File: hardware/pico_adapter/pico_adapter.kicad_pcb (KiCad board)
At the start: 2 copper layers, 97.8 x 83.8 mm, 43 parts, among them J1 L77HDE15SD1CH4F, J2 AudioJack3, J3 5V in, Q1 Q_NMOS_DGS, Q2 Q_NMOS_DGS

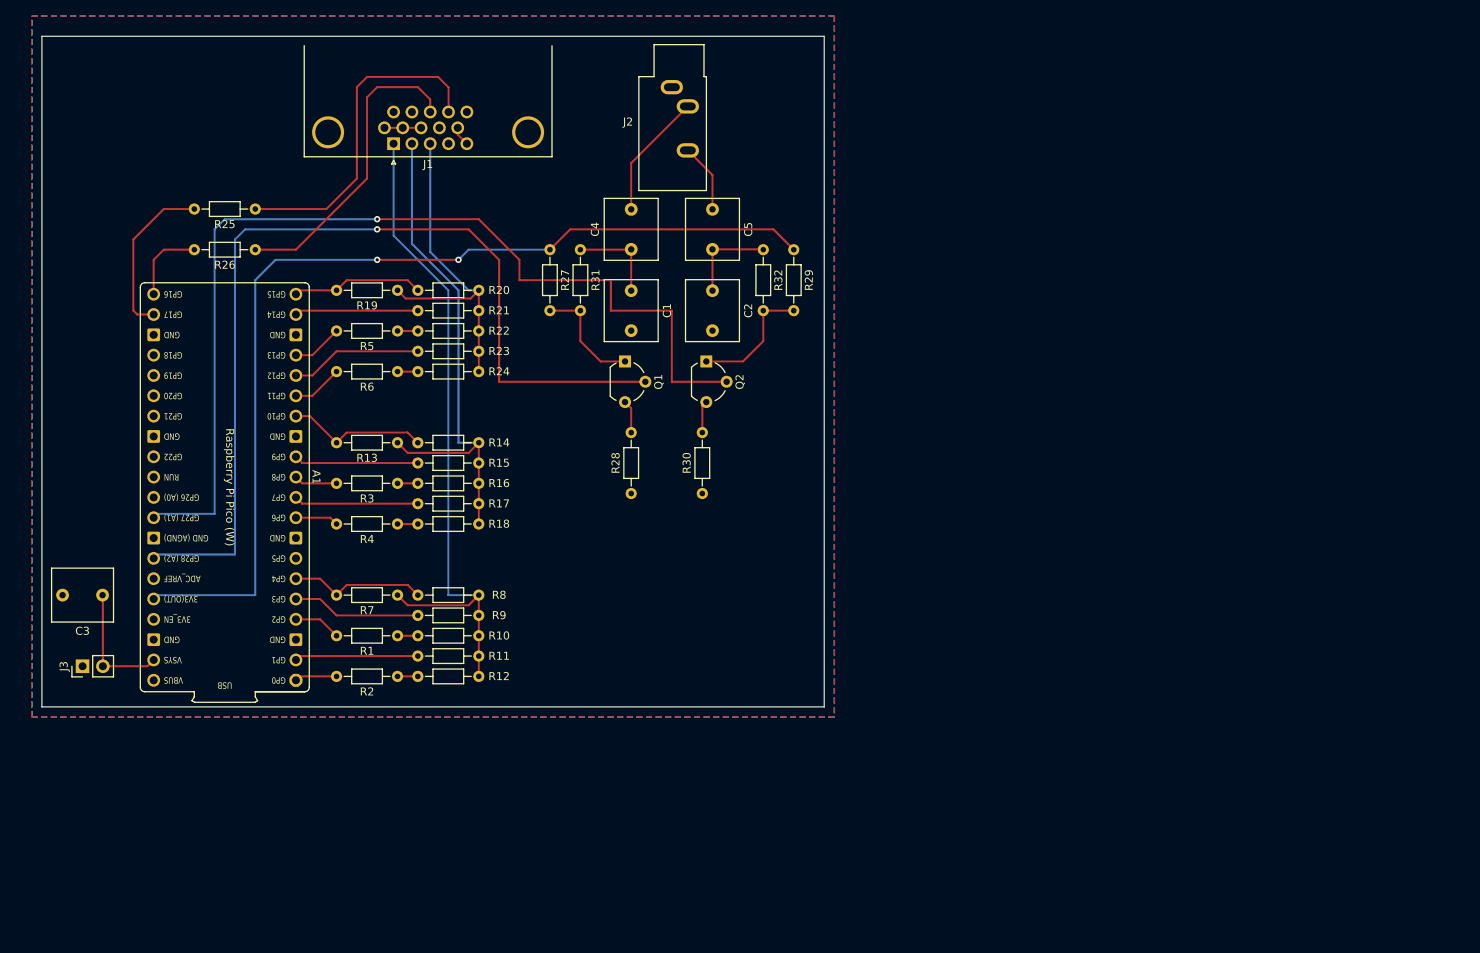
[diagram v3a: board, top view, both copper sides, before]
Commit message: UPDATED PICO FOOTPRINT [!] + smaller board
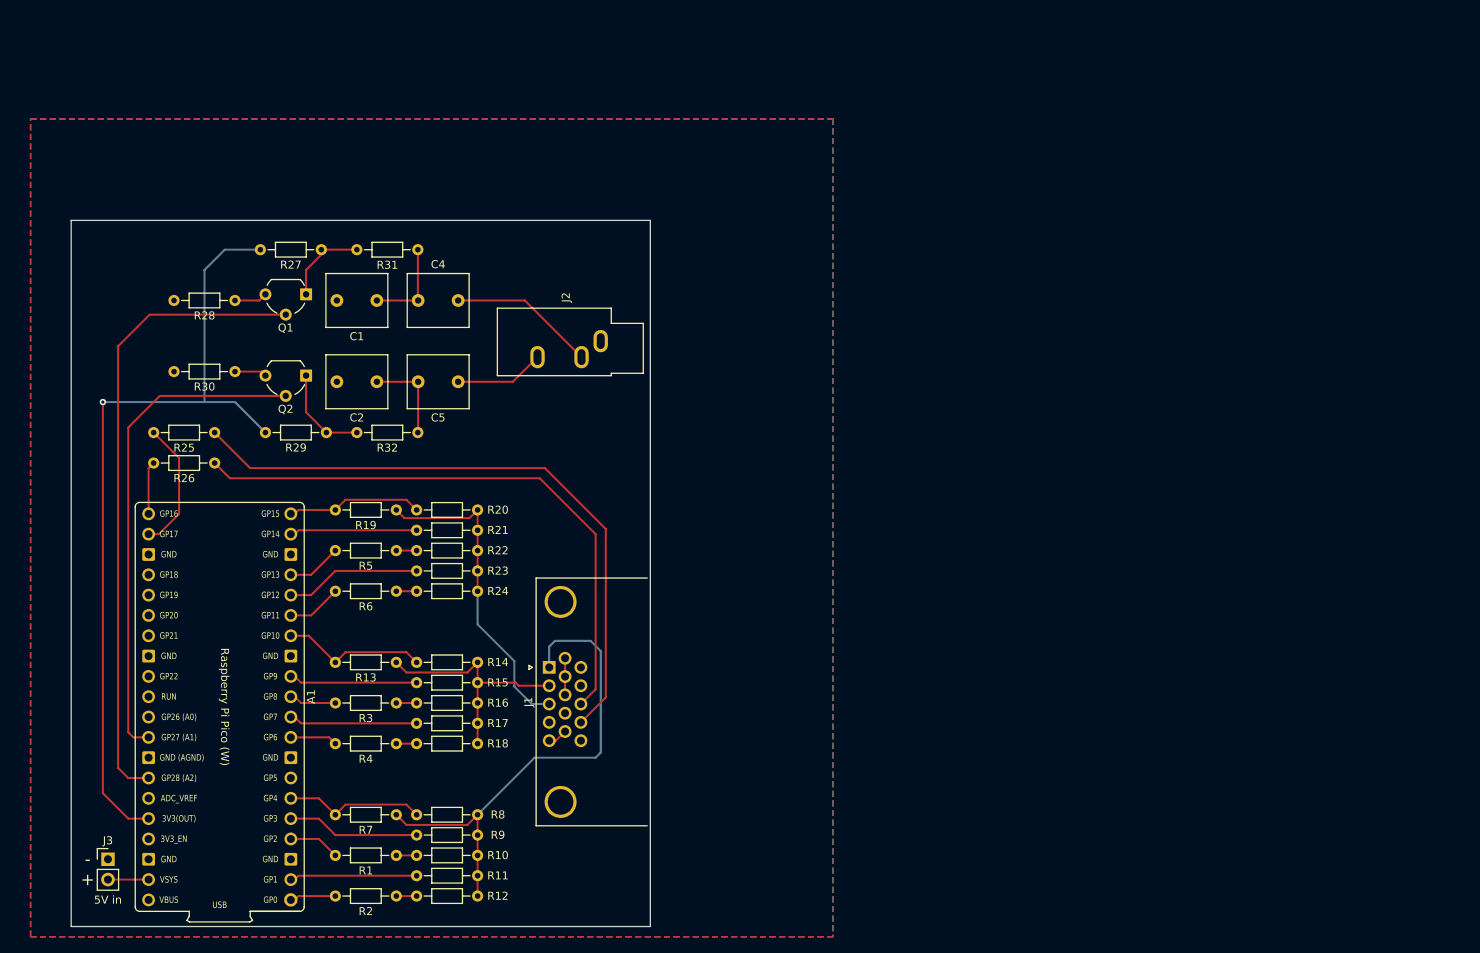
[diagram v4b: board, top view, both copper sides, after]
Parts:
- removed C3: 100n, Capacitor_THT:C_Rect_L7.5mm_W6.5mm_P5.00mm
- moved R29 69.9 mm to (59.7, 72.4), turned to 0 degrees
- moved J1 68.3 mm to (95.2, 101.7), turned to 90 degrees
- moved R30 67.8 mm to (48.3, 64.8), turned to 0 degrees
- moved R28 62.0 mm to (48.3, 55.9), turned to 0 degrees
- moved Q2 50.1 mm to (64.8, 65.3), turned to 180 degrees
- moved R32 48.9 mm to (78.7, 72.4), turned to 180 degrees
- moved C2 43.5 mm to (73.6, 66.0), turned to 180 degrees
- moved Q1 40.7 mm to (64.8, 55.1), turned to 180 degrees
- moved C5 38.4 mm to (83.8, 66.0), turned to 180 degrees
- moved R27 36.2 mm to (59.1, 49.5), turned to 0 degrees
- moved J2 33.0 mm to (101.6, 61.0), turned to -90 degrees
- moved C1 31.8 mm to (73.6, 55.9), turned to 180 degrees
- moved R25 28.4 mm to (53.3, 72.4)
- moved A1 27.5 mm to (62.9, 130.8)
- moved R18 27.5 mm to (86.2, 111.3)
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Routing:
- net /PWM_R: track 125.3 -> 62.2 mm, vias 1 -> 0
- net /PWM_L: track 118.7 -> 79.6 mm, vias 1 -> 0
- net /VSYNC: track 41.3 -> 79.3 mm
- net /HSYNC: track 38.4 -> 73.3 mm
- net /VGA_G: track 63.7 -> 30.5 mm
- net /VGA_R: track 84.4 -> 62.5 mm
- net +3V3: track 123.5 -> 102.4 mm, vias 2 -> 1
- net +5V: track 15.6 -> 5.08 mm
- net Net-(A1-Pad22): track 20.8 -> 16.3 mm
- net Net-(Q1-Pad1): track 14.3 -> 10.4 mm
- net Net-(Q2-Pad1): track 15.8 -> 12.0 mm
- net Net-(A1-Pad21): track 9.90 -> 6.61 mm
- net Net-(C5-Pad1): track 8.65 -> 11.2 mm
- net Net-(C4-Pad2): track 15.8 -> 18.4 mm
- net /VGA_B: track 42.8 -> 40.3 mm
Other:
- board size 97.8 x 83.8 mm -> 72.4 x 88.3 mm
- board text added: "+"
- board text added: "-"

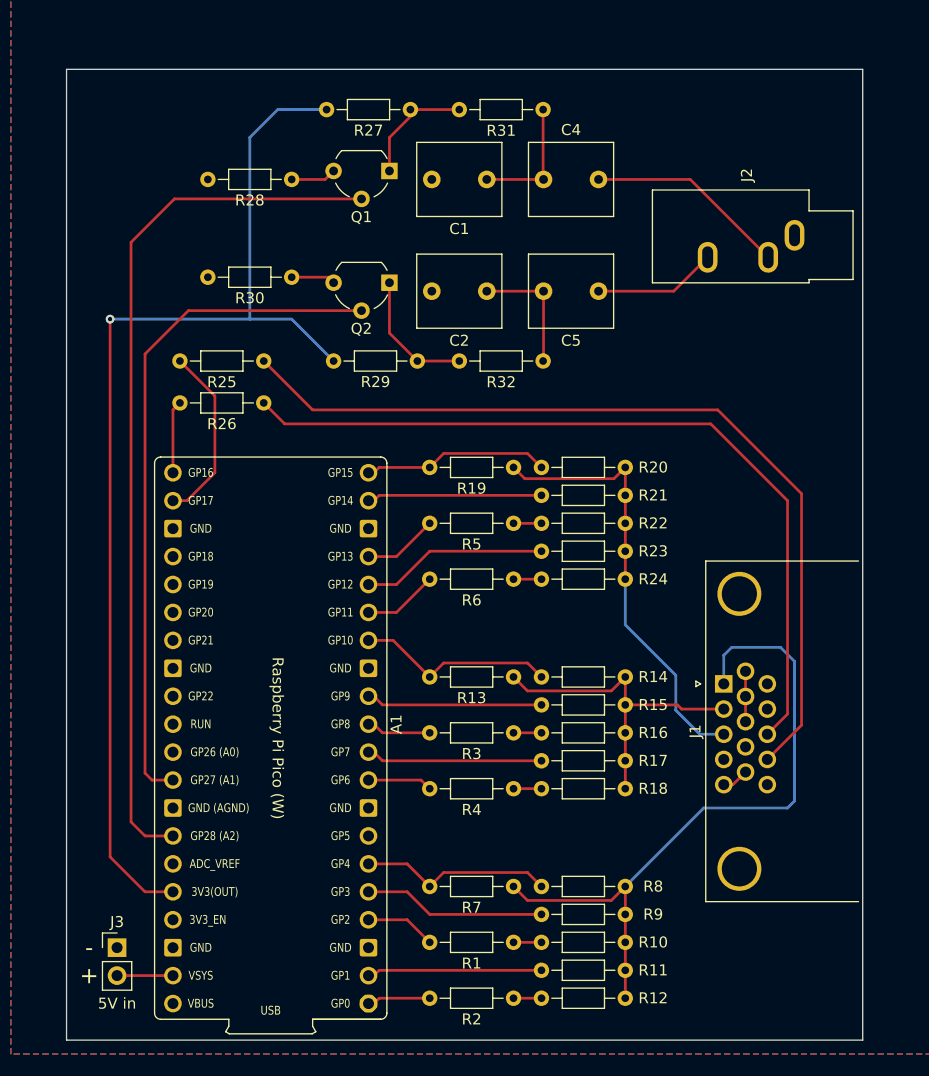
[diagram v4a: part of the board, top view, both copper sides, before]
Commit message: bigger resistors
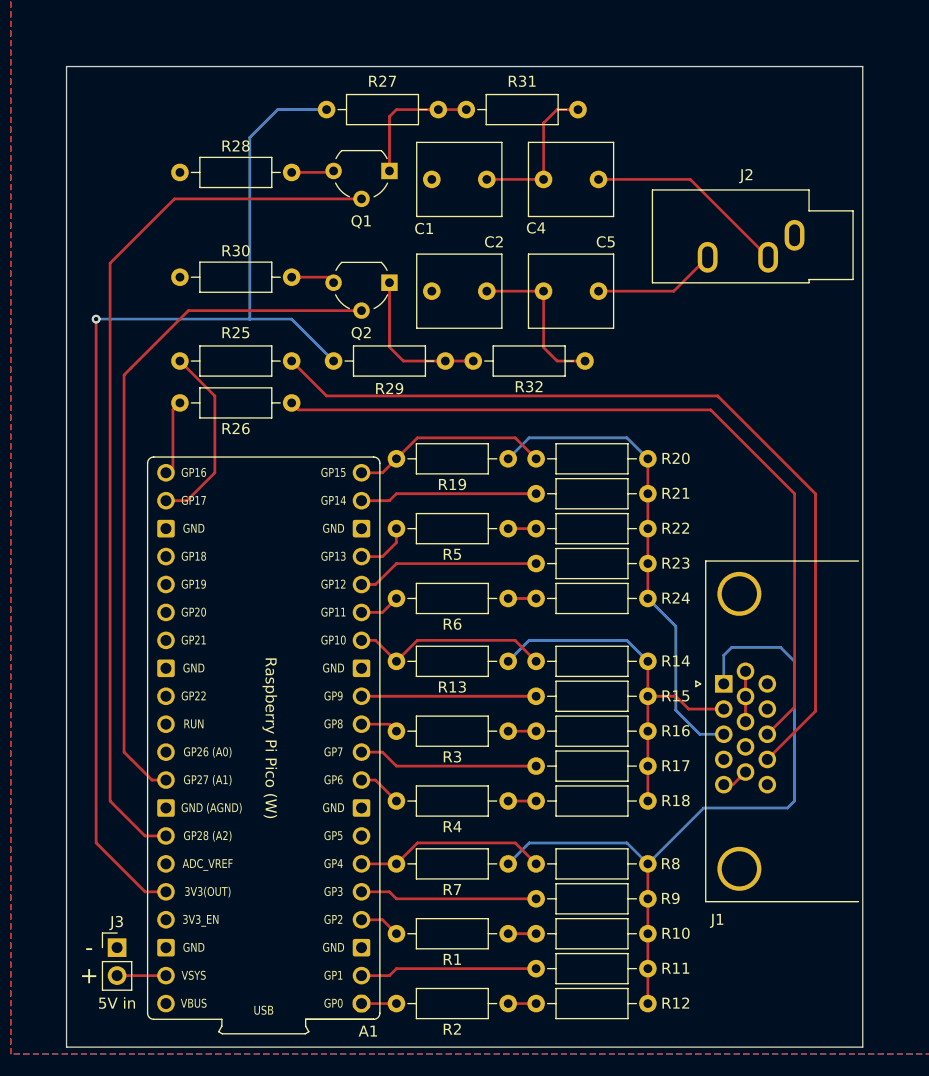
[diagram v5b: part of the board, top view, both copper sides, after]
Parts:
- R1, R10, R11, R12, R13, R14, R15, R16, R17, R18, R19, R2, R20, R21, R22, R23, R24, R25, R26, R27, R28, R29, R3, R30, R31, R32, R4, R5, R6, R7, R8, R9: footprint Resistor_THT:R_Axial_DIN0204_L3.6mm_D1.6mm_P7.62mm_Horizontal -> Resistor_THT:R_Axial_DIN0207_L6.3mm_D2.5mm_P10.16mm_Horizontal
- moved R32 3.81 mm to (82.5, 72.4)
- moved R31 3.18 mm to (81.9, 49.5)
- moved R8 2.91 mm to (88.3, 118.1)
- moved R24 2.70 mm to (88.3, 94.0)
- moved R28 2.62 mm to (45.7, 55.2)
- moved R25 2.54 mm to (55.9, 72.4)
- moved R26 2.54 mm to (55.9, 76.2)
- moved R30 2.54 mm to (45.7, 64.8)
- moved R14 2.50 mm to (88.3, 99.7)
- moved R9 2.50 mm to (88.3, 121.3)
- moved R23 2.34 mm to (88.3, 90.8)
- moved R18 2.34 mm to (88.3, 112.4)
- moved R10 2.20 mm to (88.3, 124.5)
- moved R15 2.20 mm to (88.3, 102.9)
- moved R20 2.20 mm to (88.3, 81.3)
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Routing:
- net /VGA_G: track 30.5 -> 34.4 mm
- net /VGA_B: track 40.3 -> 43.5 mm
- net Net-(C2-Pad1): track 11.5 -> 14.6 mm
- net /VGA_R: track 62.5 -> 65.2 mm
- net /GPIO11: track 6.33 -> 3.70 mm
- net Net-(C1-Pad1): track 11.5 -> 13.9 mm
- net /GPIO2: track 5.93 -> 3.70 mm
- net /GPIO0: track 5.28 -> 3.18 mm
- net Net-(Q2-Pad1): track 12.0 -> 14.0 mm
- net /GPIO8: track 5.41 -> 3.44 mm
- net Net-(Q1-Pad1): track 10.4 -> 12.2 mm
- net /GPIO15: track 16.5 -> 18.0 mm
- net /GPIO6: track 5.41 -> 3.96 mm
- net /GPIO13: track 6.33 -> 4.97 mm
- net /HSYNC: track 73.3 -> 72.0 mm
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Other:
- board size 72.4 x 88.3 mm -> 72.4 x 89.2 mm

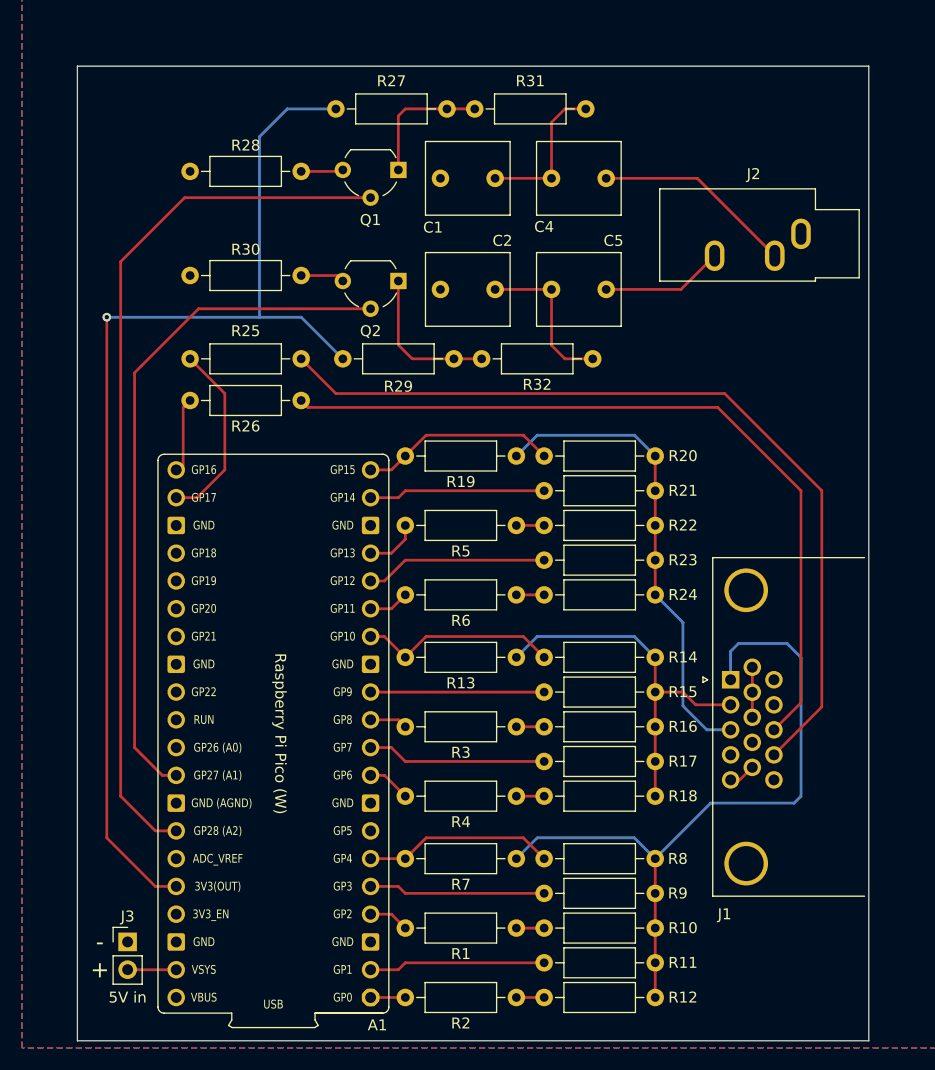
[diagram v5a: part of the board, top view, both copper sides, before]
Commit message: added addon-headers + reset button
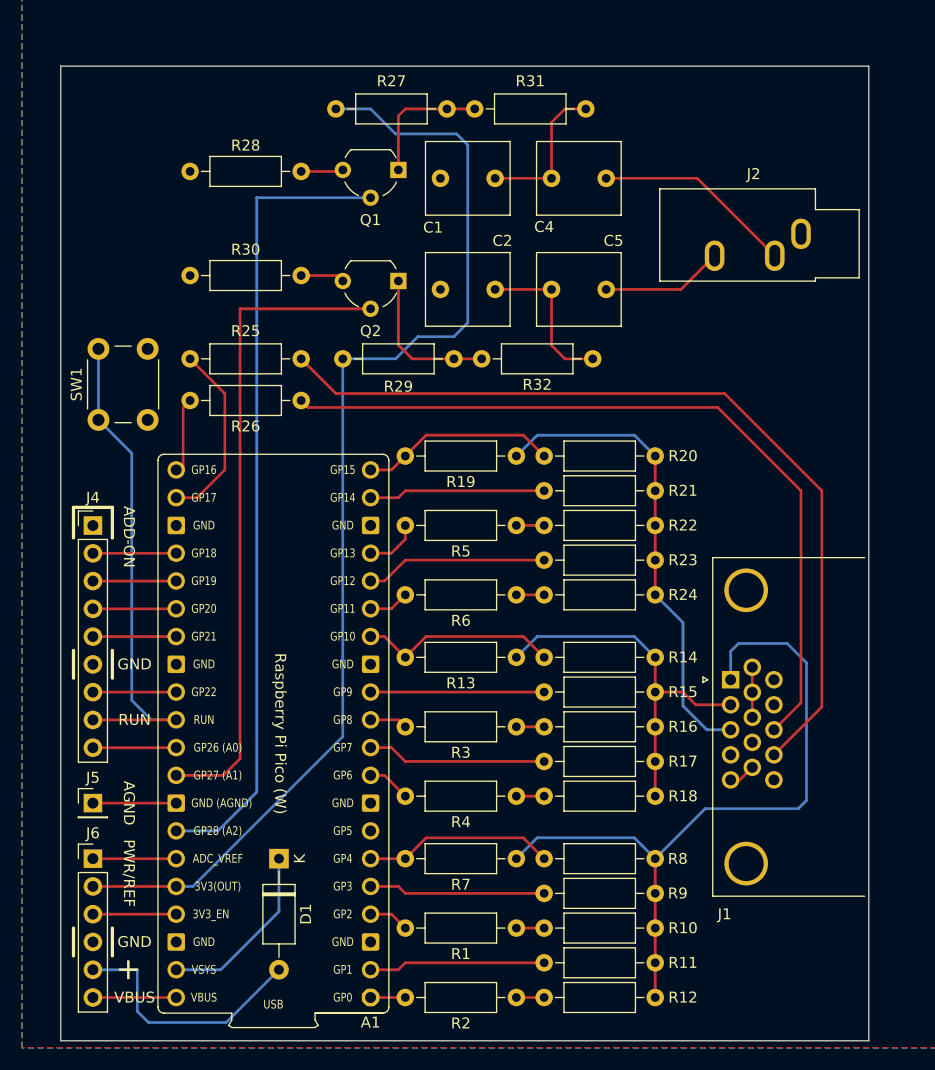
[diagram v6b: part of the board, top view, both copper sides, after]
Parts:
- removed J3: 5V in, Connector_PinHeader_2.54mm:PinHeader_1x02_P2.54mm_Vertical
- added D1: D_Schottky, Diode_THT:D_A-405_P10.16mm_Horizontal, F.Cu at (53.8, 118.1)
- added J4: ADD-ON, Connector_PinHeader_2.54mm:PinHeader_1x09_P2.54mm_Vertical, F.Cu at (36.8, 87.6)
- added J5: AGND, Connector_PinHeader_2.54mm:PinHeader_1x01_P2.54mm_Vertical, F.Cu at (36.8, 113.0)
- added J6: PWR_REF, Connector_PinHeader_2.54mm:PinHeader_1x06_P2.54mm_Vertical, F.Cu at (36.8, 118.1)
- added SW1: SW_Push, Button_Switch_THT:SW_PUSH_6mm_H5mm, F.Cu at (37.3, 78.0)
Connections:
- net Net-(A1-Pad21) renamed /GPIO16
- net Net-(A1-Pad22) renamed /GPIO17
- A1 pad 24: unconnected-(A1-Pad24) -> /GPIO18
- A1 pad 25: unconnected-(A1-Pad25) -> /GPIO19
- A1 pad 26: unconnected-(A1-Pad26) -> /GPIO20
- A1 pad 27: unconnected-(A1-Pad27) -> /GPIO21
- A1 pad 29: unconnected-(A1-Pad29) -> /GPIO22
- A1 pad 30: unconnected-(A1-Pad30) -> /RUN
- A1 pad 31: unconnected-(A1-Pad31) -> /GPIO26
- A1 pad 33: unconnected-(A1-Pad33) -> /AGND
- A1 pad 35: unconnected-(A1-Pad35) -> /ADC_VREF
- A1 pad 37: unconnected-(A1-Pad37) -> /3V3_EN
- A1 pad 39: +5V -> Net-(A1-Pad39)
- A1 pad 40: unconnected-(A1-Pad40) -> /VBUS
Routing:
- net /RUN: track 0.00 -> 45.8 mm
- net +5V: track 4.45 -> 23.2 mm
- net Net-(A1-Pad39): track 0.00 -> 16.4 mm
- net /GPIO20: track 0.00 -> 7.62 mm
- net /GPIO19: track 0.00 -> 7.62 mm
- net /GPIO18: track 0.00 -> 7.62 mm
- net /GPIO26: track 0.00 -> 7.62 mm
- net /GPIO22: track 0.00 -> 7.62 mm
- net /GPIO21: track 0.00 -> 7.62 mm
- net /VBUS: track 0.00 -> 7.62 mm
- net /AGND: track 0.00 -> 7.62 mm
- net /ADC_VREF: track 0.00 -> 7.62 mm
- net /3V3_EN: track 0.00 -> 7.62 mm
- net /PWM_L: track 80.6 -> 73.6 mm
- net /PWM_R: track 63.2 -> 59.6 mm
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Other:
- board size 72.4 x 89.2 mm -> 73.9 x 89.2 mm
- board text added: "ADD-ON"
- board text added: "AGND"
- board text added: "GND"
- board text added: "PWR/REF"
- board text added: "RUN"
- board text added: "VBUS"
- board text removed: "-"
